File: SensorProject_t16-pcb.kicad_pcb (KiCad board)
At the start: 2 copper layers, 48.1 x 71.1 mm, 97 parts, among them J1 Conn_01x02_Pin, J10 Conn_01x02_Pin, J11 Conn_01x02_Pin, J12 Conn_01x02_Pin, J13 Conn_01x02_Pin, J14 Conn_01x02_Pin, J15 Conn_01x02_Pin, J16 Conn_01x02_Pin, J18 Conn_02x04_Top_Bottom, J2 Conn_01x02_Pin, J20 Screw_Terminal_01x02, J3 Conn_01x02_Pin, J4 Conn_01x02_Pin, J5 Conn_01x02_Pin, J6 Conn_01x02_Pin, J7 Conn_01x02_Pin, J8 Conn_01x02_Pin, J9 Conn_01x02_Pin, SW1 SW_Push, SW2 SW_Push, U1 ADS1115IDGS, U2 ADS1115IDGS, U3 ADS1115IDGS, U4 ADS1115IDGS, U5 STM32F411CEU6, U6 AMS1117-3.3 SOT-223, U7 RFM95W-915S2, Y1 25MHz, Y2 32.758kHz

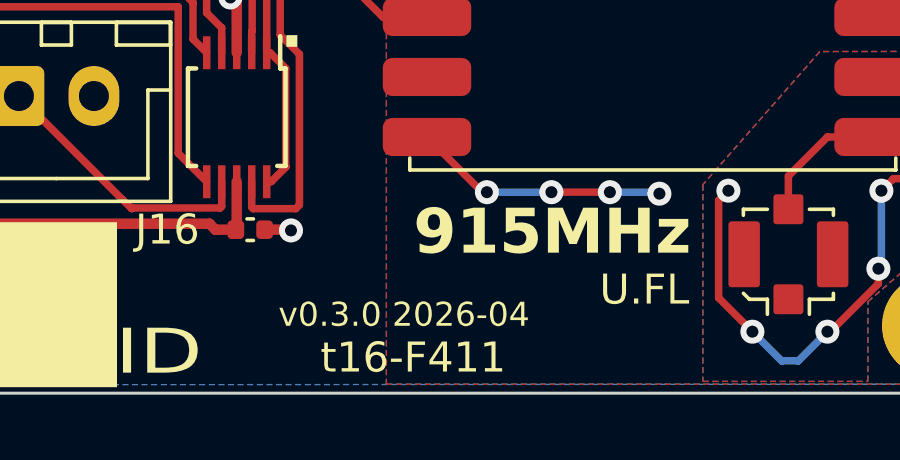
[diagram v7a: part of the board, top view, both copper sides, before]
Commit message: added QR and ID blocks on silkscreen. Marked HSE and LSE as DNP. Revised version number to 0.3.1.
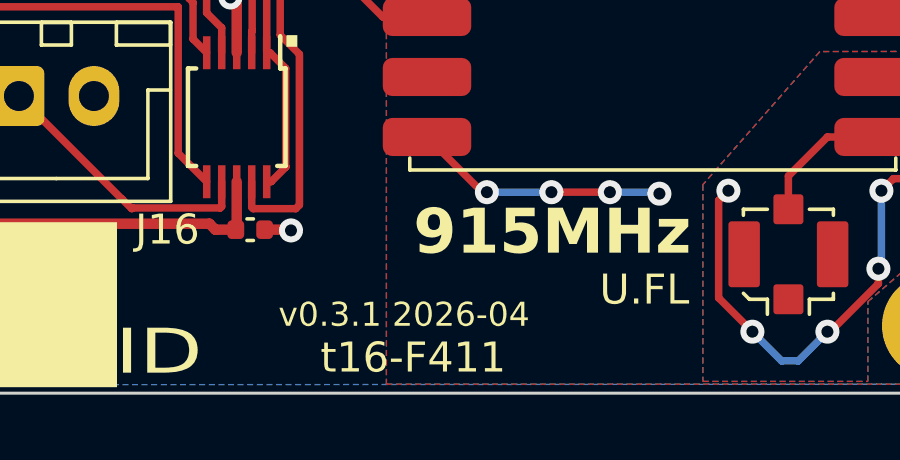
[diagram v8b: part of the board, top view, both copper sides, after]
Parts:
- C14: value 4.7µF -> 4.7uF
- C5: value 1µF -> 1uF
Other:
- board text added: "v0.3.1 2026-04"
- board text removed: "v0.3.0 2026-04"
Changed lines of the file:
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@@
 			)
 		)
-		(attr smd)
+		(attr smd exclude_from_pos_files dnp)
 		(duplicate_pad_numbers_are_jumpers no)
 		(fp_line
@@
 		(tags "capacitor")
 		(property "Reference" "C13"
-			(at 0 -1.16 225)
+			(at 0 -1.16 45)
 			(layer "F.SilkS")
 			(hide yes)
@@
 		)
 		(property "Value" "4pF C0G, NP0, +/- 0.1pF"
-			(at -10.168194 0.933384 225)
+			(at -10.168194 0.933384 45)
 			(layer "F.Fab")
 			(effects
@@
 		)
 		(property "Datasheet" ""
-			(at 0 0 225)
+			(at 0 0 45)
 			(layer "F.Fab")
 			(hide yes)
@@
 		)
 		(property "Description" "Unpolarized capacitor"
-			(at 0 0 225)
+			(at 0 0 45)
 			(layer "F.Fab")
 			(hide yes)
@@
 			)
 		)
-		(attr smd)
+		(attr smd exclude_from_pos_files dnp)
 		(duplicate_pad_numbers_are_jumpers no)
 		(fp_line
@@
 		)
 		(fp_text user "${REFERENCE}"
-			(at 0 0 225)
+			(at 0 0 45)
 			(layer "F.Fab")
 			(effects
@@
 			)
 		)
-		(attr smd)
+		(attr smd exclude_from_pos_files dnp)
 		(duplicate_pad_numbers_are_jumpers no)
 		(fp_line
@@
 			)
 		)
+		(property "Package" "none"
+			(at 0 0 0)
+			(unlocked yes)
+			(layer "F.Fab")
+			(hide yes)
+			(effects
+				(font
+					(size 1 1)
+					(thickness 0.15)
+				)
+			)
+		)
 		(property ki_fp_filters "Pin* Test*")
 		(sheetname "/f411/")
@@
 			)
 		)
-		(attr dnp)
+		(attr exclude_from_pos_files exclude_from_bom dnp)
 		(duplicate_pad_numbers_are_jumpers no)
 		(fp_circle
@@
 			)
 		)
-		(property "Package" ""
+		(property "Package" "none"
 			(at 0 0 0)
 			(unlocked yes)
@@
 			)
 		)
-		(attr dnp)
+		(attr exclude_from_pos_files exclude_from_bom dnp)
 		(duplicate_pad_numbers_are_jumpers no)
 		(fp_circle
@@
 		(tags "capacitor")
 		(property "Reference" "C10"
-			(at 0 -1.16 225)
+			(at 0 -1.16 45)
 			(layer "F.SilkS")
 			(hide yes)
@@
 		)
 		(property "Value" "10pF C0G, NP0, +/- 0.1pF"
-			(at -8.188297 -0.056569 225)
+			(at -8.188297 -0.056569 45)
 			(layer "F.Fab")
 			(effects
@@
 		)
 		(property "Datasheet" ""
-			(at 0 0 225)
+			(at 0 0 45)
 			(layer "F.Fab")
 			(hide yes)
@@
 		)
 		(property "Description" "Unpolarized capacitor"
-			(at 0 0 225)
+			(at 0 0 45)
 			(layer "F.Fab")
 			(hide yes)
@@
 			)
 		)
-		(attr smd)
+		(attr smd exclude_from_pos_files dnp)
 		(duplicate_pad_numbers_are_jumpers no)
 		(fp_line
@@
 		)
 		(fp_text user "${REFERENCE}"
-			(at 0 0 225)
+			(at 0 0 45)
 			(layer "F.Fab")
 			(effects
@@
 		(tags "capacitor")
 		(property "Reference" "C11"
-			(at 0 -1.16 315)
+			(at 0 -1.16 135)
 			(layer "F.SilkS")
 			(hide yes)
@@
 		)
 		(property "Datasheet" ""
-			(at 0 0 315)
+			(at 0 0 135)
 			(layer "F.Fab")
 			(hide yes)
@@
 		)
 		(property "Description" "Unpolarized capacitor"
-			(at 0 0 315)
+			(at 0 0 135)
 			(layer "F.Fab")
 			(hide yes)
@@
 			)
 		)
-		(attr smd)
+		(attr smd exclude_from_pos_files dnp)
 		(duplicate_pad_numbers_are_jumpers no)
 		(fp_line
@@
 		)
 		(fp_text user "${REFERENCE}"
-			(at 0 0 315)
+			(at 0 0 135)
 			(layer "F.Fab")
 			(effects
@@
 		(tags "capacitor")
 		(property "Reference" "C5"
-			(at 0 -1.16 270)
+			(at 0 -1.16 90)
 			(layer "F.SilkS")
 			(hide yes)
@@
 			)
 		)
-		(property "Value" "1µF"
-			(at -0.960001 -0.869997 225)
+		(property "Value" "1uF"
+			(at -0.960001 -0.869997 45)
 			(layer "F.Fab")
 			(effects
@@
 		)
 		(property "Datasheet" ""
-			(at 0 0 270)
+			(at 0 0 90)
 			(layer "F.Fab")
 			(hide yes)
@@
 		)
 		(property "Description" "Unpolarized capacitor"
-			(at 0 0 270)
+			(at 0 0 90)
 			(layer "F.Fab")
 			(hide yes)
@@
 		)
 		(fp_text user "${REFERENCE}"
-			(at 0 0 270)
+			(at 0 0 90)
 			(layer "F.Fab")
 			(effects
@@
 		(tags "capacitor")
 		(property "Reference" "C14"
-			(at 0 -1.16 270)
+			(at 0 -1.16 90)
 			(layer "F.SilkS")
 			(hide yes)
@@
 			)
 		)
-		(property "Value" "4.7µF"
-			(at -0.830001 -1.289997 225)
+		(property "Value" "4.7uF"
+			(at -0.830001 -1.289997 45)
 			(layer "F.Fab")
 			(effects
@@
 		)
 		(property "Datasheet" ""
-			(at 0 0 270)
+			(at 0 0 90)
 			(layer "F.Fab")
 			(hide yes)
@@
 		)
 		(property "Description" "Unpolarized capacitor"
-			(at 0 0 270)
+			(at 0 0 90)
 			(layer "F.Fab")
 			(hide yes)
@@
 		)
 		(fp_text user "${REFERENCE}"
-			(at 0 0 270)
+			(at 0 0 90)
 			(layer "F.Fab")
 			(effects
@@
 			)
 		)
-		(attr smd)
+		(attr smd exclude_from_pos_files dnp)
 		(duplicate_pad_numbers_are_jumpers no)
 		(fp_line
@@
 			)
 		)
-		(attr smd)
+		(attr smd exclude_from_pos_files dnp)
 		(duplicate_pad_numbers_are_jumpers no)
 		(fp_line
@@
 		(tags "capacitor")
 		(property "Reference" "C12"
-			(at 0 -1.16 225)
+			(at 0 -1.16 45)
 			(layer "F.SilkS")
 			(hide yes)
@@
 		)
 		(property "Value" "4pF C0G, NP0, +/- 0.1pF"
-			(at -10.344971 0.64347 225)
+			(at -10.344971 0.64347 45)
 			(layer "F.Fab")
 			(effects
@@
 		)
 		(property "Datasheet" ""
-			(at 0 0 225)
+			(at 0 0 45)
 			(layer "F.Fab")
 			(hide yes)
@@
 		)
 		(property "Description" "Unpolarized capacitor"
-			(at 0 0 225)
+			(at 0 0 45)
 			(layer "F.Fab")
 			(hide yes)
@@
 			)
 		)
-		(attr smd)
+		(attr smd exclude_from_pos_files dnp)
 		(duplicate_pad_numbers_are_jumpers no)
 		(fp_line
@@
 		)
 		(fp_text user "${REFERENCE}"
-			(at 0 0 225)
+			(at 0 0 45)
 			(layer "F.Fab")
 			(effects
@@
 			)
 		)
-		(attr smd)
+		(attr smd exclude_from_pos_files dnp)
 		(duplicate_pad_numbers_are_jumpers no)
 		(fp_line
@@
 		(layer "Edge.Cuts")
 	)
-	(gr_text "v0.3.0 2026-04"
+	(gr_text "v0.3.1 2026-04"
 		(at 73.479997 93.099999 0)
 		(layer "F.SilkS")
